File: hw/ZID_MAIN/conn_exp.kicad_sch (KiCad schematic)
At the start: 67 parts, among them J10 USB-C PWR ONLY, J11 Conn_01x08, J8 BRK-EXP-UNIT, J9 Z80-TARGET, U24 74AHCT00

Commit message: BP-EXP: 1 board only. PLCC-DIP: Adapter form.
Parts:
- J8: JTAG_NOTE1 (none) -> SHORT 39-40; JTAG_NOTE2 (none) -> for JTAG-ISP
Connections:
- net +5V: now also J8.2 (PWR), J8.4 (PWR), J8.6 (PWR); no longer J8.40 (PWR)
- net AEN_CLK: now also J8.27 (AECLK); no longer J8.21 (AECLK)
- net AEN_CLR-: now also J8.29 (~{AECLR}); no longer J8.23 (~{AECLR})
- net BA_CLK: now also J8.23 (ADCLK); no longer J8.17 (ADCLK)
- net BA_CLR-: now also J8.25 (~{ADCLR}); no longer J8.19 (~{ADCLR})
- net BRK2N_AEQ-: now also J8.30 (~{ADEQ}); no longer J8.27 (~{ADEQ})
- net BRKHW_DET-: now also J8.28 (~{UNITDET}); no longer J8.25 (~{UNITDET})
- net D7_B: now also J8.24 (ADDI), J8.26 (AEDI); no longer J8.18 (ADDI1), J8.28 (AEDI1)
- net GND: now also J8.1 (GND), J8.3 (GND), J8.5 (GND); no longer J8.38 (GND), J8.39 (GND)
- net LA0: now also J8.8 (A0); no longer J8.2 (A0)
- net LA1: now also J8.7 (A1); no longer J8.1 (A1)
- net LA10: now also J8.18 (A10); no longer J8.12 (A10)
- net LA11: now also J8.17 (A11); no longer J8.11 (A11)
- net LA12: now also J8.20 (A12); no longer J8.14 (A12)
- net LA13: now also J8.19 (A13); no longer J8.13 (A13)
- net LA14: now also J8.22 (A14); no longer J8.16 (A14)
- net LA15: now also J8.21 (A15); no longer J8.15 (A15)
- net LA2: now also J8.10 (A2); no longer J8.4 (A2)
- net LA3: now also J8.9 (A3); no longer J8.3 (A3)
- net LA4: now also J8.12 (A4); no longer J8.6 (A4)
- net LA5: now also J8.11 (A5); no longer J8.5 (A5)
- net LA6: now also J8.14 (A6); no longer J8.8 (A6)
- net LA7: now also J8.13 (A7); no longer J8.7 (A7)
- net LA8: now also J8.16 (A8); no longer J8.10 (A8)
- net LA9: now also J8.15 (A9); no longer J8.9 (A9)
- net TIORQ-: now also J8.35 (~{IORQ}); no longer J8.33 (~{IORQ})
- net TM1-: now also J8.31 (~{M1}); no longer J8.29 (~{M1})
- net TMREQ-: now also J8.33 (~{MREQ}); no longer J8.31 (~{MREQ})
- net TRD-: now also J8.34 (~{RD}); no longer J8.37 (~{RD})
- net TRST-: no longer U24.10, U24.13, U24.2, U24.5
- net TWR-: now also J8.36 (~{WR}); no longer J8.35 (~{WR})
- net ZRFSH-: now also J8.32 (~{RFSH})
- new net JTCK: J8.37 (JTCK)
- new net JTD2O3I: J8.39 (JTDI_CO)
- new net JTDO_CI: J8.40 (JTDO_CI)
- new net JTMS: J8.38 (JTMS)
- new net LRST-: U24.10, U24.13, U24.2, U24.5
- no-connect marks 16 -> 8
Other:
- moved on the sheet: C16, C18, C20, C22, R19, R20, SPARE1

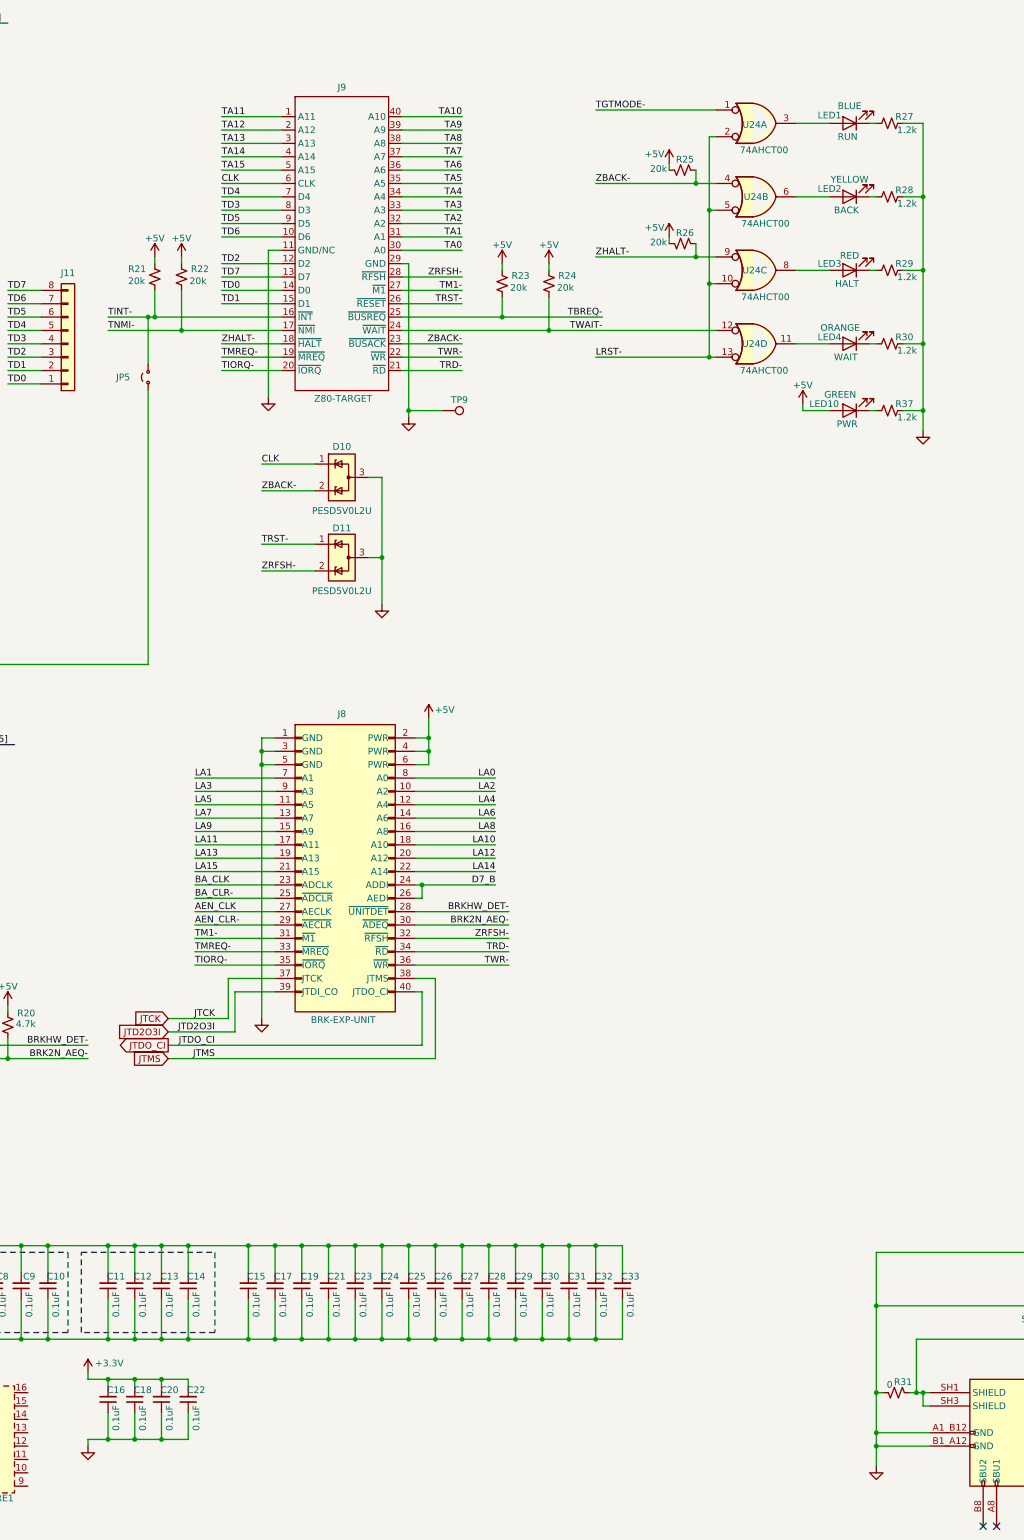
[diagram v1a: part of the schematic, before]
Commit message: Change ZID,POD,ExpBP connector to SIP
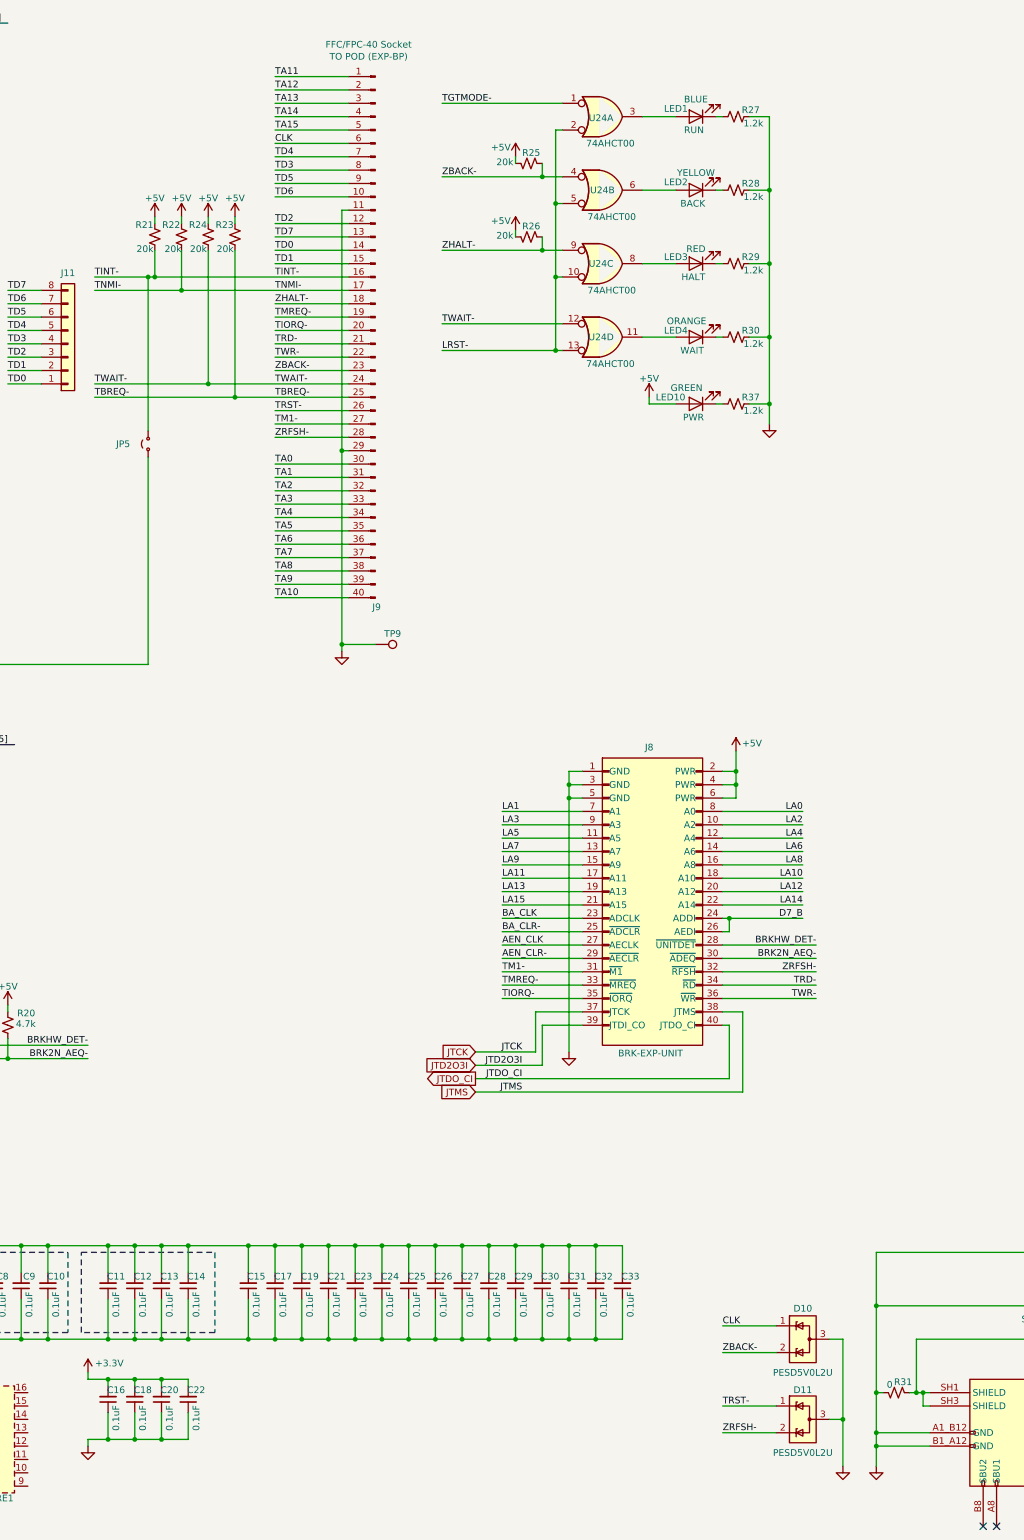
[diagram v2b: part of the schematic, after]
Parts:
- removed J9: Z80-TARGET, AES_Library:CviLux_CF25401D0-05-NH_FFC-FPC-AES, symbol AES_Library:Z80-Target-AES
- added J9: FFC/FPC-40 Socket, symbol Connector:Conn_01x40_Pin
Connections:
- net CLK: now also J9.6 (Pin_6)
- net GND: now also J9.11 (Pin_11), J9.29 (Pin_29)
- net TA0: now also J9.30 (Pin_30)
- net TA1: now also J9.31 (Pin_31)
- net TA10: now also J9.40 (Pin_40)
- net TA11: now also J9.1 (Pin_1)
- net TA12: now also J9.2 (Pin_2)
- net TA13: now also J9.3 (Pin_3)
- net TA14: now also J9.4 (Pin_4)
- net TA15: now also J9.5 (Pin_5)
- net TA2: now also J9.32 (Pin_32)
- net TA3: now also J9.33 (Pin_33)
- net TA4: now also J9.34 (Pin_34)
- net TA5: now also J9.35 (Pin_35)
- net TA6: now also J9.36 (Pin_36)
- net TA7: now also J9.37 (Pin_37)
- net TA8: now also J9.38 (Pin_38)
- net TA9: now also J9.39 (Pin_39)
- net TBREQ-: now also J9.25 (Pin_25)
- net TD0: now also J9.14 (Pin_14)
- net TD1: now also J9.15 (Pin_15)
- net TD2: now also J9.12 (Pin_12)
- net TD3: now also J9.8 (Pin_8)
- net TD4: now also J9.7 (Pin_7)
- net TD5: now also J9.9 (Pin_9)
- net TD6: now also J9.10 (Pin_10)
- net TD7: now also J9.13 (Pin_13)
- net TINT-: now also J9.16 (Pin_16)
- net TIORQ-: now also J9.20 (Pin_20)
- net TM1-: now also J9.27 (Pin_27)
- net TMREQ-: now also J9.19 (Pin_19)
- net TNMI-: now also J9.17 (Pin_17)
- net TRD-: now also J9.21 (Pin_21)
- net TRST-: now also J9.26 (Pin_26)
- net TWAIT-: now also J9.24 (Pin_24)
- net TWR-: now also J9.22 (Pin_22)
- net ZBACK-: now also J9.23 (Pin_23)
- net ZHALT-: now also J9.18 (Pin_18)
- net ZRFSH-: now also J9.28 (Pin_28)
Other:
- moved on the sheet: D10, D11, J8, JP5, LED1, LED10, LED2, LED3, LED4, R21, R22, R23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

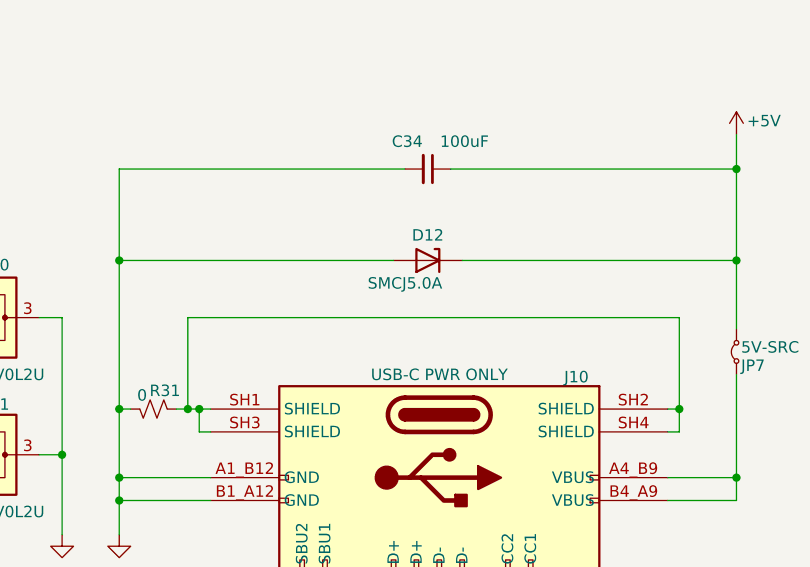
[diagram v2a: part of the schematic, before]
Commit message: ZID Main: TVS from SMC5.0 to SMA6.0
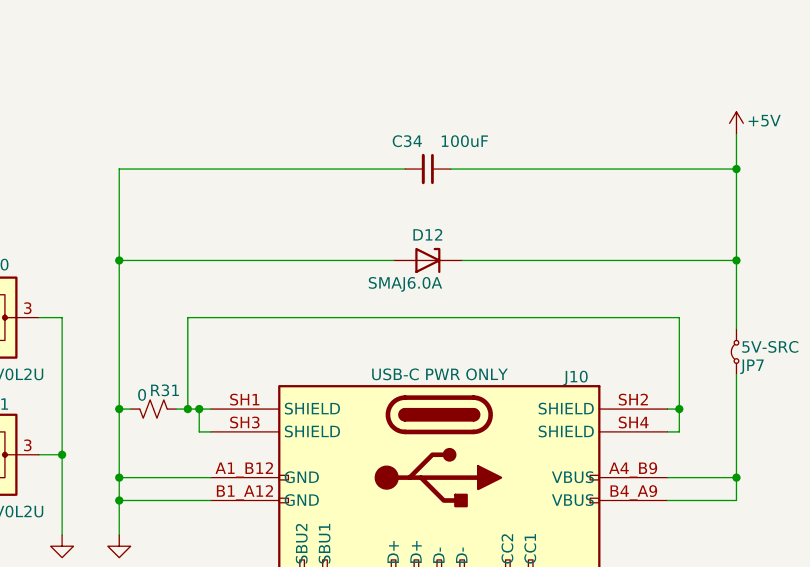
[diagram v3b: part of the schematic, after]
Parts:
- D12: value SMCJ5.0A -> SMAJ6.0A; footprint Diode_SMD:D_SOD-523 -> Diode_SMD:D_SMA
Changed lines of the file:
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@@
 	(title_block
 		(title "Target Pod and Break Expand")
-		(date "2026-04-18")
+		(date "2026-04-19")
 		(rev "PR-1.0")
 		(company "SilkyDESIGN / CMOS1")
@@
 			)
 		)
-		(property "Value" "SMCJ5.0A"
+		(property "Value" "SMAJ6.0A"
 			(at 254 266.7 0)
 			(effects
@@
 			)
 		)
-		(property "Footprint" "Diode_SMD:D_SOD-523"
+		(property "Footprint" "Diode_SMD:D_SMA"
 			(at 256.54 268.605 0)
 			(effects
@@
 			)
 		)
-		(property "Description" "ESD Protection Diode, SOD-523"
+		(property "Description" "ESD Protection Diode, DO-214AC package"
 			(at 256.54 264.16 0)
 			(effects

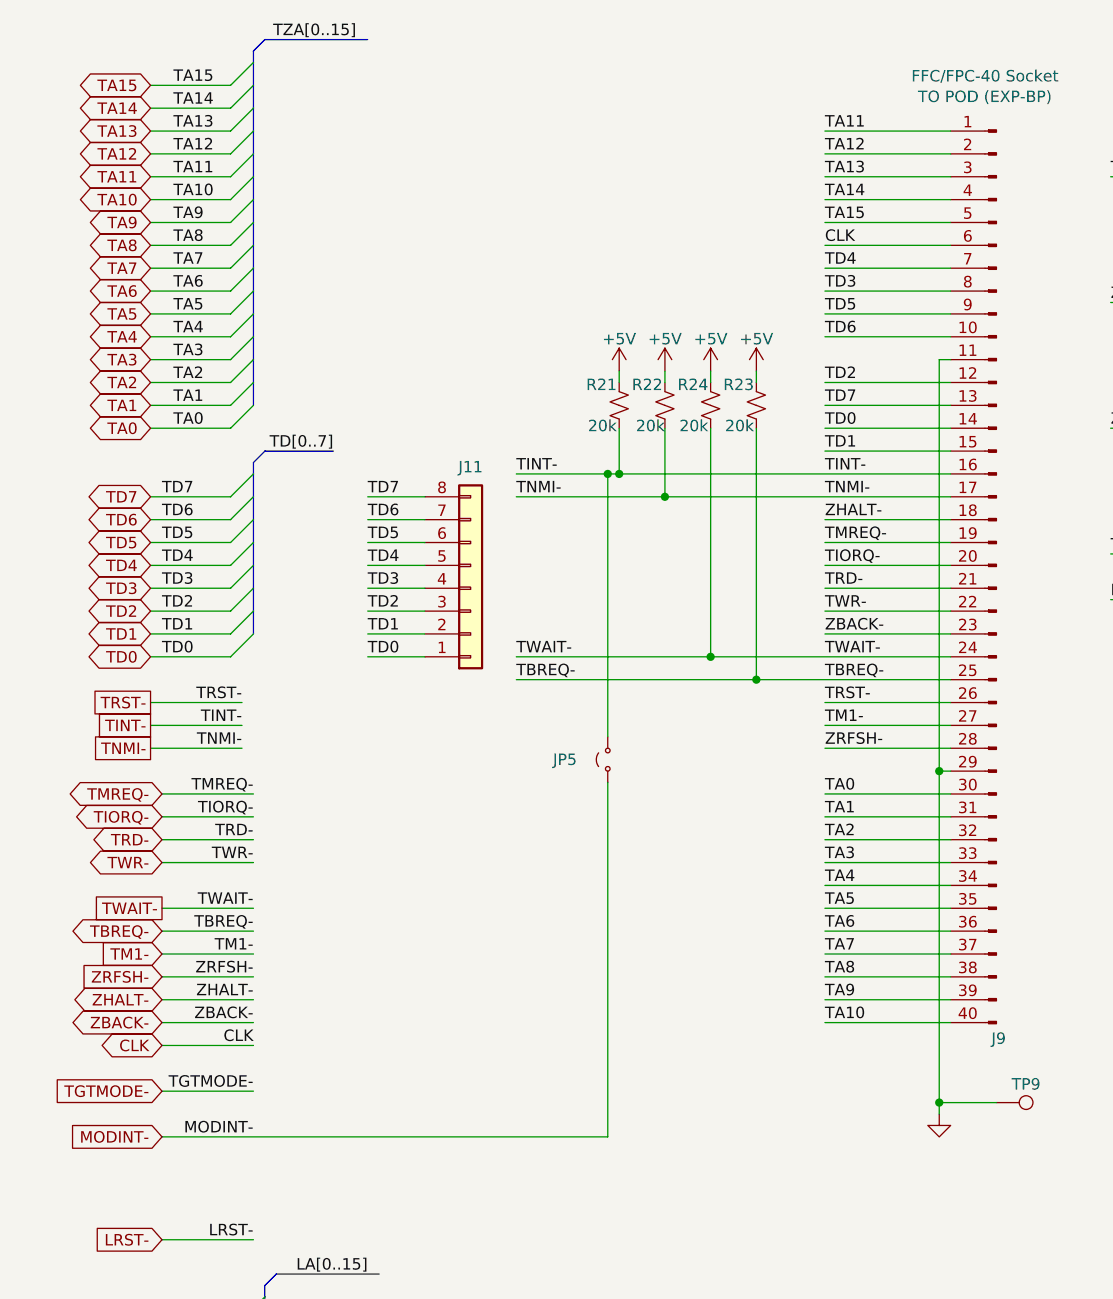
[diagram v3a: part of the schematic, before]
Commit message: 74FCT541 to 74FCT2245. Move GND around CLK on ZID-POD connector
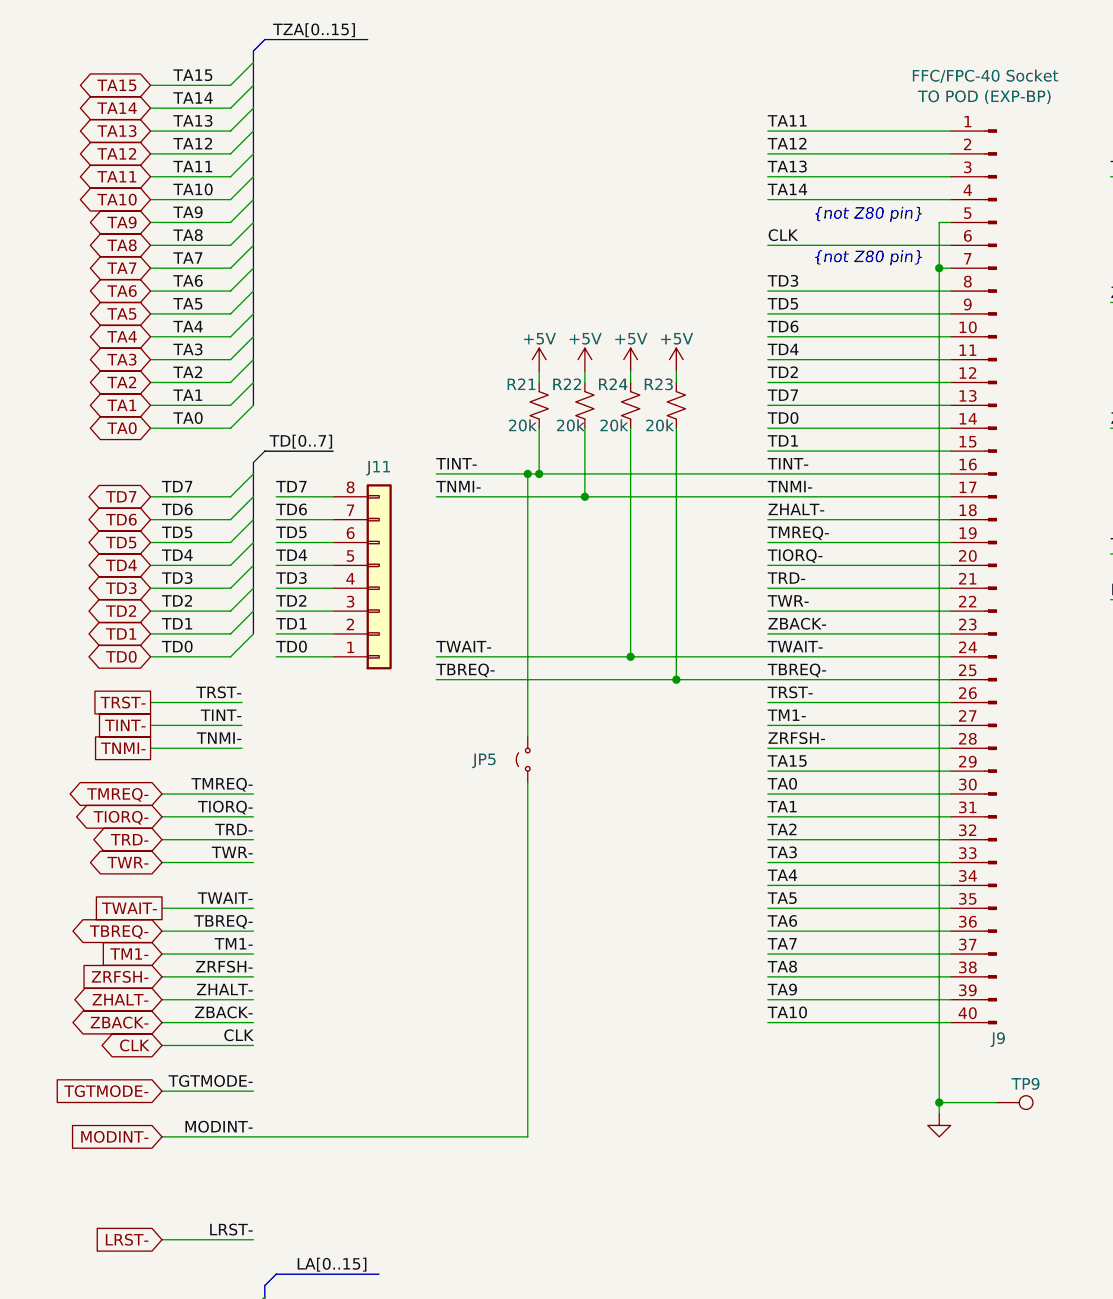
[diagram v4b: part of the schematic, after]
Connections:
- net GND: now also J9.5 (Pin_5), J9.7 (Pin_7); no longer J9.11 (Pin_11), J9.29 (Pin_29)
- net TA15: now also J9.29 (Pin_29); no longer J9.5 (Pin_5)
- net TD4: now also J9.11 (Pin_11); no longer J9.7 (Pin_7)
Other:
- note added: "{not Z80 pin}"
- moved on the sheet: J11, JP5, R21, R22, R23, R24

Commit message: SCHM: Update CPLD pins and put all break units on board.
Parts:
- LED1: value LED BLUE -> LED GREEN; footprint LED_THT:LED_D3.0mm -> LED_SMD:LED_0805_2012Metric; Ind BLUE -> GREEN
- LED10: value LED ORANGE -> LED BLUE; footprint LED_THT:LED_D3.0mm -> LED_SMD:LED_0805_2012Metric; Ind GREEN -> BLUE
- LED2: value LED YELLOW -> LED ORANGE; footprint LED_THT:LED_D3.0mm -> LED_SMD:LED_0805_2012Metric; Ind YELLOW -> ORANGE
- LED3: footprint LED_THT:LED_D3.0mm -> LED_SMD:LED_0805_2012Metric
- LED4: value LED ORANGE -> LED YELLOW; footprint LED_THT:LED_D3.0mm -> LED_SMD:LED_0805_2012Metric; Ind ORANGE -> YELLOW
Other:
- moved on the sheet: C10, C11, C12, C13, C14, C15, C16, C17, C18, C19, C20, C21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
